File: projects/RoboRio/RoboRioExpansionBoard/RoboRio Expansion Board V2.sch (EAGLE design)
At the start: 82 parts, among them J1 RRINTERFACE-FEMALE, J2 MICROSD, Q1 5.0 MHz, T1 NPN-SOT416, U1 P8X32A-Q44, U2 24LC256ST, U3 FT232RFTR232R, U4 MC1525TO

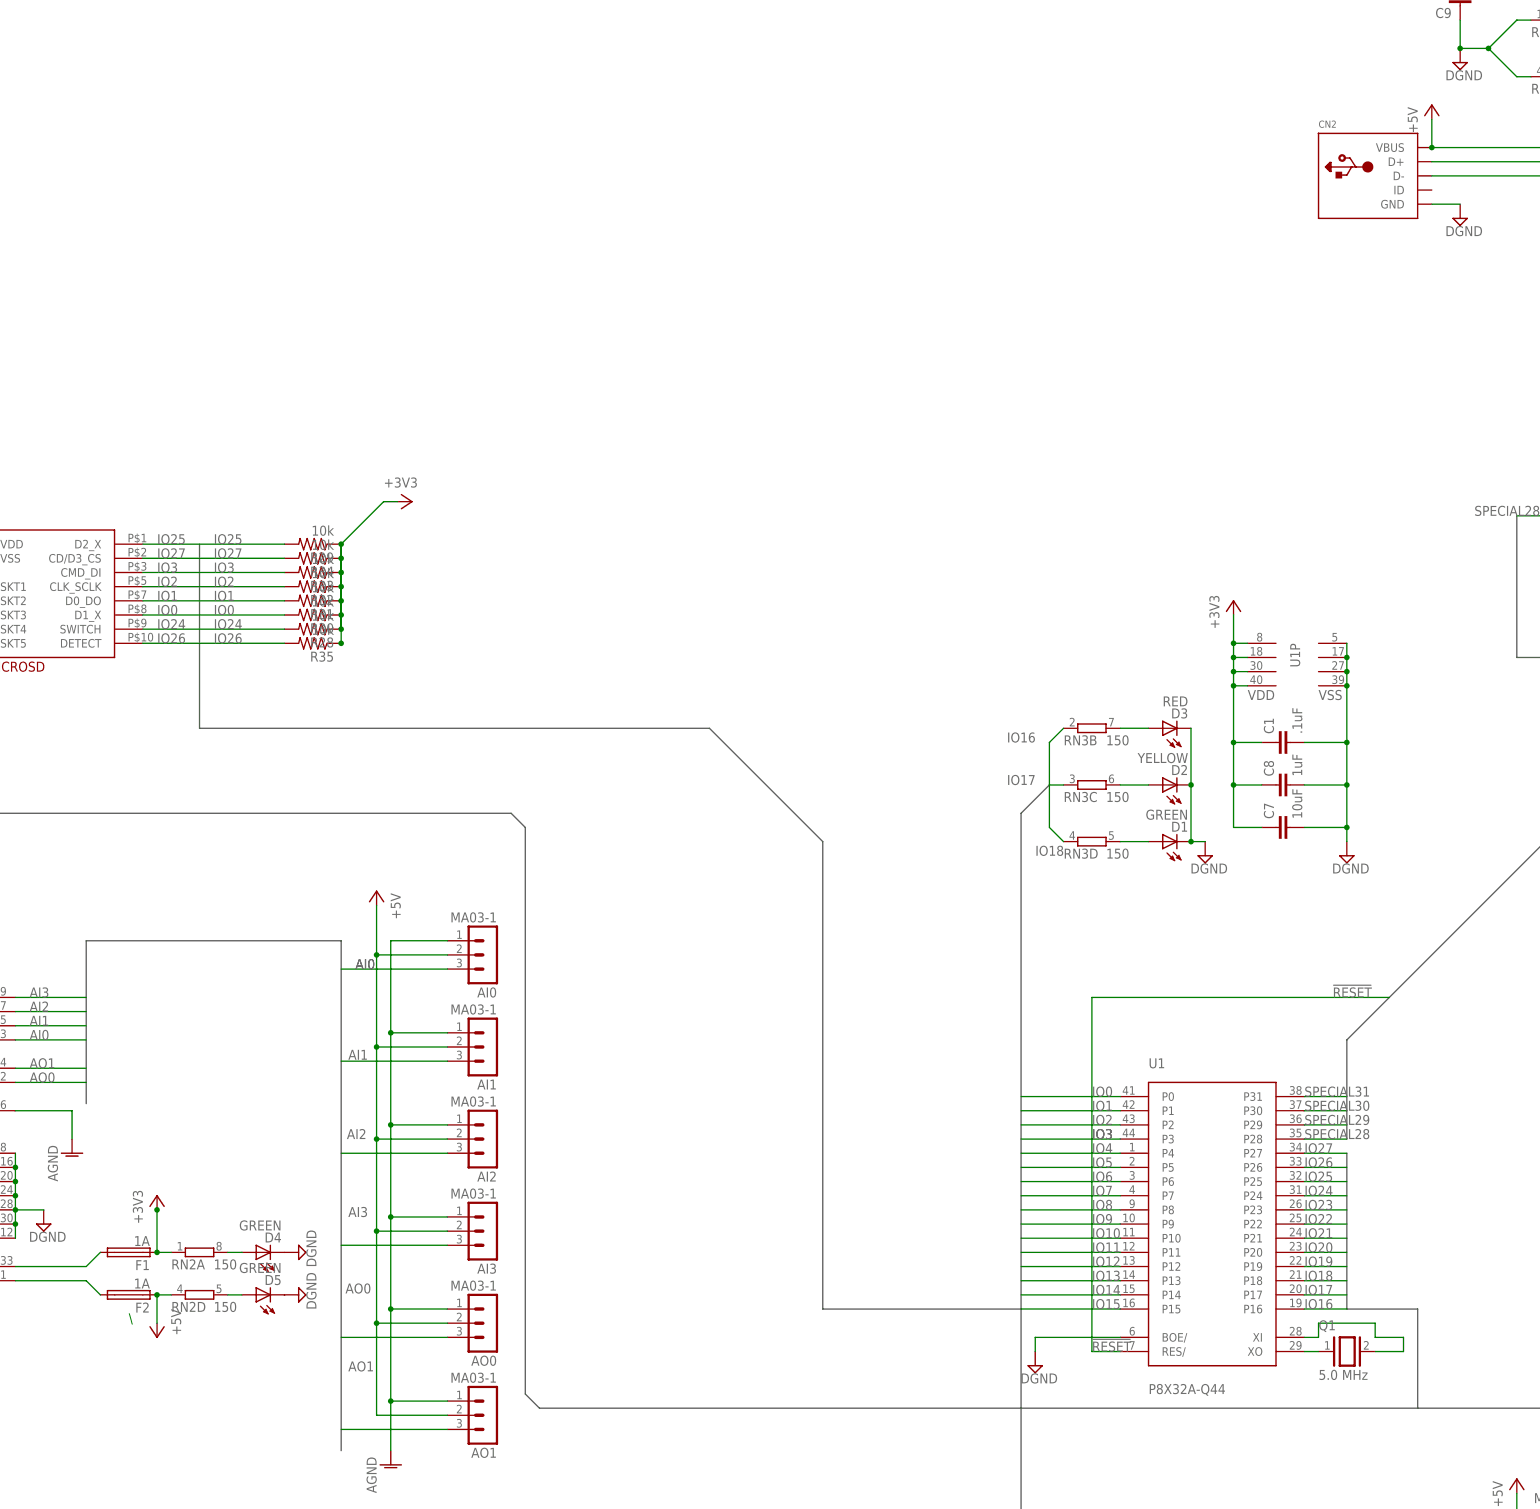
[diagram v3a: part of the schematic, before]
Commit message: Small changes
Made more space by moving stuff around
USB 5V is no longer directly tied to RR 5V
Removed fuses
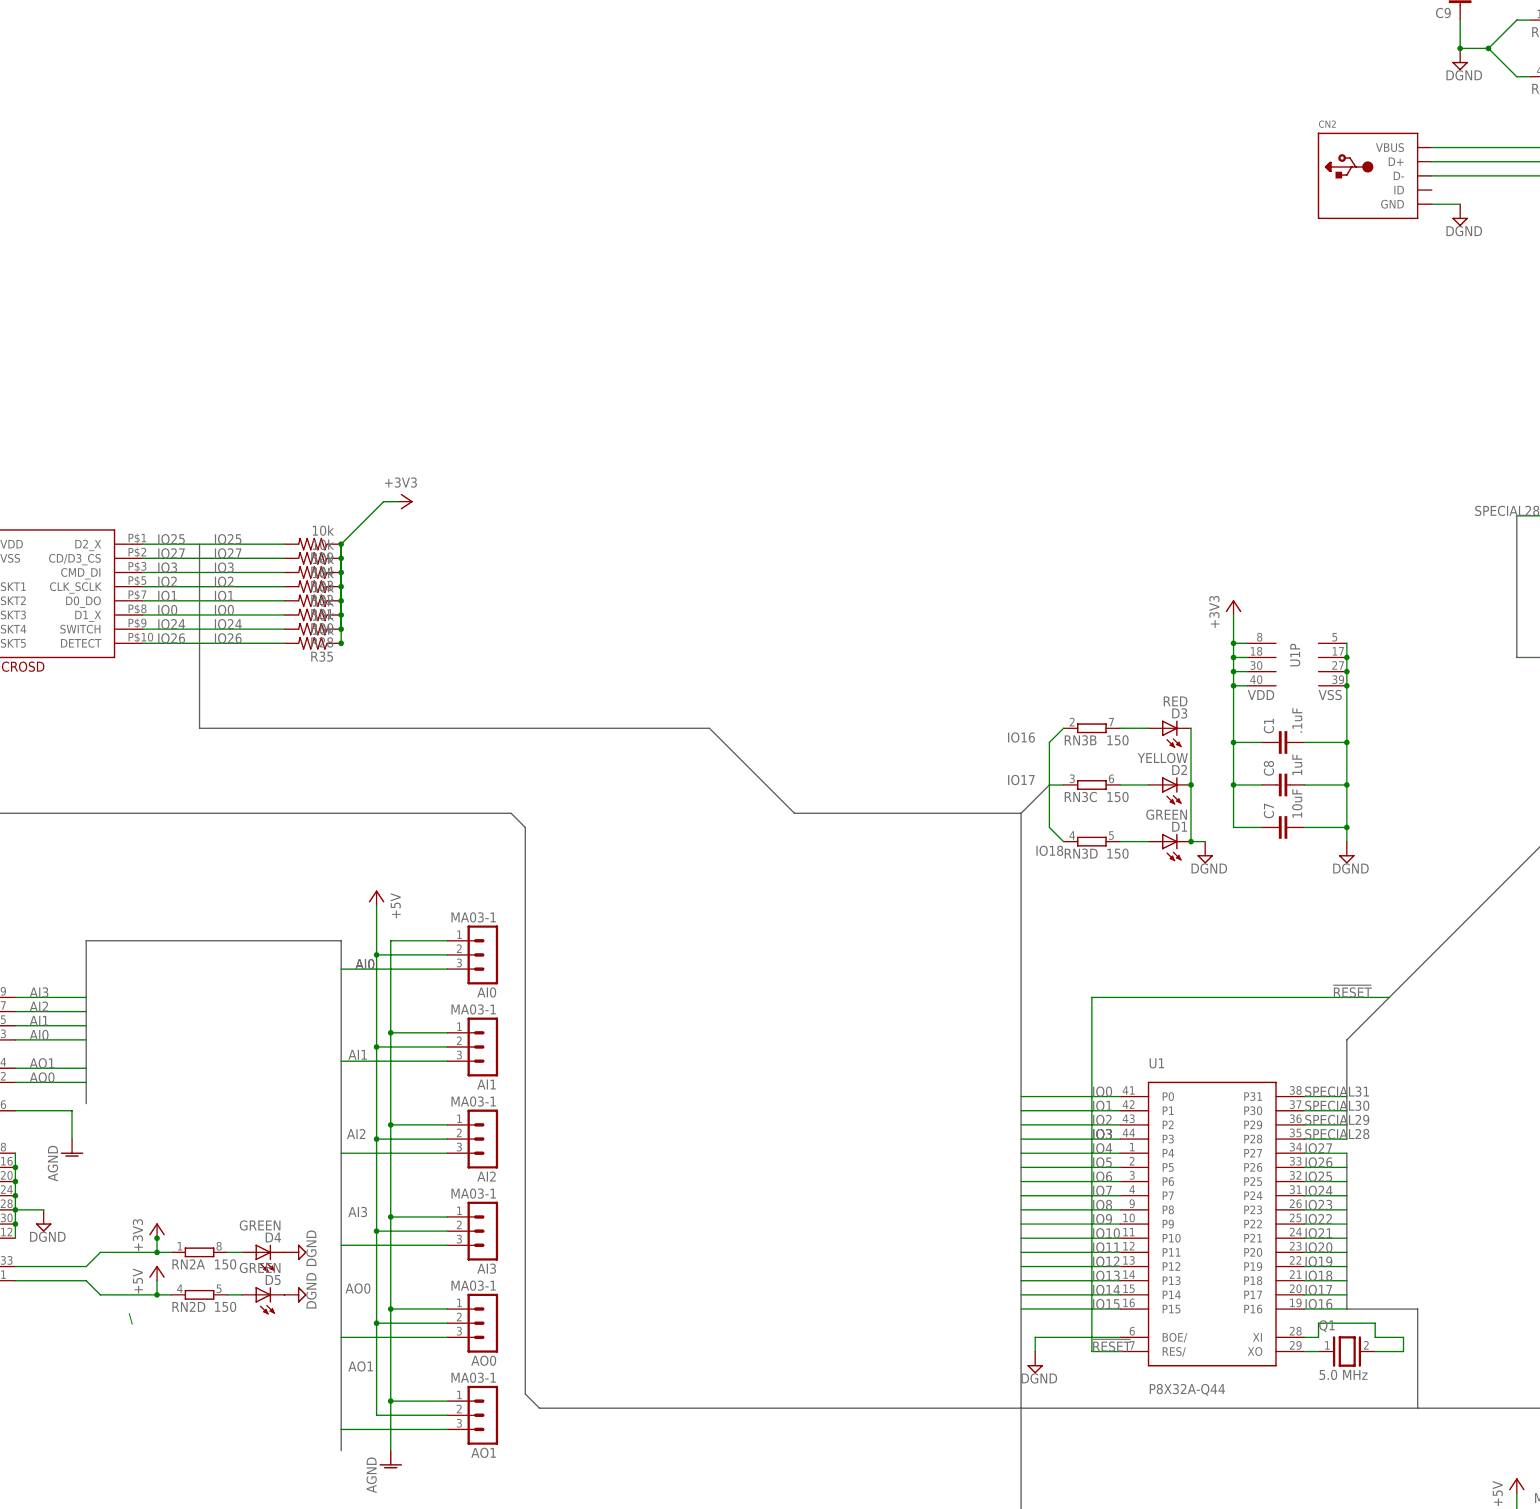
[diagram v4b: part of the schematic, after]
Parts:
- removed F1, F2: 1A, fuse:TR5
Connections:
- removed net N$15: F2.2, J1.P1-5V
- net +3V3: now also J1.P33-+3.3V; no longer F1.1
- net +5V: now also J1.P1-5V; no longer CN2.VBUS, F2.1, U3.VCC
- net N$5: now also CN2.VBUS, U3.VCC; no longer F1.2, J1.P33-+3.3V
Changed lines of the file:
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@@
 <part name="ADC7" library="con-lstb-modified" deviceset="MA03-1" device=""/>
 <part name="P+14" library="supply1" deviceset="+5V" device=""/>
-<part name="F2" library="fuse" deviceset="TR5" device="" value="1A"/>
-<part name="F1" library="fuse" deviceset="TR5" device="" value="1A"/>
 <part name="D4" library="led" deviceset="LED" device="CHIPLED_0603" value="GREEN"/>
 <part name="D5" library="led" deviceset="LED" device="CHIPLED_0603" value="GREEN"/>
@@
 <part name="U5" library="MAX11621EEE" deviceset="MAXIM1152" device="SMT"/>
 <part name="CN2" library="adafruit" deviceset="USB" device="MINIB"/>
-<part name="P+1" library="supply1" deviceset="+5V" device=""/>
 <part name="U3" library="FT232R" deviceset="FT232R" device="FTR232R"/>
 <part name="C9" library="resistor" deviceset="C-EU" device="C0603K" value="1uF"/>
@@
 <instance part="ADC7" gate="G$1" x="271.78" y="-66.04" rot="R180"/>
 <instance part="P+14" gate="1" x="256.54" y="-59.69"/>
-<instance part="F2" gate="1" x="-160.02" y="20.32" rot="R180"/>
-<instance part="F1" gate="1" x="-160.02" y="27.94" rot="R180"/>
 <instance part="D4" gate="G$1" x="-137.16" y="27.94" rot="R90"/>
 <instance part="D5" gate="G$1" x="-137.16" y="20.32" rot="R90"/>
 <instance part="SUPPLY39" gate="G$1" x="-129.54" y="20.32" rot="R90"/>
 <instance part="SUPPLY40" gate="G$1" x="-129.54" y="27.94" rot="R90"/>
-<instance part="+3V7" gate="G$1" x="-154.94" y="38.1"/>
-<instance part="P+16" gate="1" x="-154.94" y="12.7" rot="R180"/>
+<instance part="+3V7" gate="G$1" x="-154.94" y="33.02"/>
+<instance part="P+16" gate="1" x="-154.94" y="25.4"/>
 <instance part="GPIO0" gate="G$1" x="127" y="66.04" rot="R180"/>
 <instance part="+3V3" gate="G$1" x="116.84" y="66.04" rot="R90"/>
@@
 <instance part="U5" gate="G$1" x="88.9" y="-76.2"/>
 <instance part="CN2" gate="G$1" x="63.5" y="220.98"/>
-<instance part="P+1" gate="1" x="73.66" y="233.68"/>
 <instance part="U3" gate="G$1" x="134.62" y="231.14"/>
 <instance part="C9" gate="G$1" x="78.74" y="251.46" rot="R180"/>
@@
 <wire x1="101.6" y1="0" x2="71.12" y2="0" width="0.762" layer="92"/>
 <wire x1="71.12" y1="0" x2="0" y2="0" width="0.762" layer="92"/>
-<wire x1="0" y1="0" x2="0" y2="17.78" width="0.762" layer="92"/>
-<wire x1="0" y1="17.78" x2="0" y2="106.68" width="0.762" layer="92"/>
+<wire x1="0" y1="0" x2="0" y2="106.68" width="0.762" layer="92"/>
 <wire x1="0" y1="106.68" x2="5.08" y2="111.76" width="0.762" layer="92"/>
 <wire x1="0" y1="0" x2="-86.36" y2="0" width="0.762" layer="92"/>
 <wire x1="-86.36" y1="0" x2="-88.9" y2="2.54" width="0.762" layer="92"/>
 <wire x1="-88.9" y1="2.54" x2="-88.9" y2="104.14" width="0.762" layer="92"/>
-<wire x1="-35.56" y1="17.78" x2="0" y2="17.78" width="0.762" layer="92"/>
+<wire x1="-40.64" y1="106.68" x2="0" y2="106.68" width="0.762" layer="92"/>
 <wire x1="0" y1="0" x2="0" y2="-50.8" width="0.762" layer="92"/>
 <wire x1="101.6" y1="0" x2="162.56" y2="0" width="0.762" layer="92"/>
@@
 <wire x1="71.12" y1="17.78" x2="58.42" y2="17.78" width="0.762" layer="92"/>
 <wire x1="58.42" y1="17.78" x2="58.42" y2="45.72" width="0.762" layer="92"/>
-<wire x1="-35.56" y1="17.78" x2="-35.56" y2="101.6" width="0.762" layer="92"/>
-<wire x1="-35.56" y1="101.6" x2="-55.88" y2="121.92" width="0.762" layer="92"/>
+<wire x1="-40.64" y1="106.68" x2="-55.88" y2="121.92" width="0.762" layer="92"/>
 <wire x1="-55.88" y1="121.92" x2="-147.32" y2="121.92" width="0.762" layer="92"/>
 <wire x1="-147.32" y1="121.92" x2="-147.32" y2="154.94" width="0.762" layer="92"/>
@@
 <pinref part="+3V7" gate="G$1" pin="+3V3"/>
 <pinref part="+3V7" gate="G$1" pin="+3V3"/>
-<pinref part="F1" gate="1" pin="1"/>
+<wire x1="-152.4" y1="27.94" x2="-154.94" y2="27.94" width="0.1524" layer="91"/>
+<wire x1="-154.94" y1="27.94" x2="-154.94" y2="30.48" width="0.1524" layer="91"/>
+<junction x="-154.94" y="30.48"/>
+<pinref part="RN2" gate="A" pin="1"/>
+<pinref part="J1" gate="G$1" pin="P33-+3.3V"/>
+<wire x1="-180.34" y1="25.4" x2="-167.64" y2="25.4" width="0.1524" layer="91"/>
+<wire x1="-167.64" y1="25.4" x2="-165.1" y2="27.94" width="0.1524" layer="91"/>
+<wire x1="-154.94" y1="27.94" x2="-165.1" y2="27.94" width="0.1524" layer="91"/>
 <junction x="-154.94" y="27.94"/>
-<wire x1="-152.4" y1="27.94" x2="-154.94" y2="27.94" width="0.1524" layer="91"/>
-<wire x1="-154.94" y1="27.94" x2="-154.94" y2="35.56" width="0.1524" layer="91"/>
-<junction x="-154.94" y="35.56"/>
-<pinref part="RN2" gate="A" pin="1"/>
 </segment>
 <segment>
@@
 </segment>
 <segment>
-<pinref part="F2" gate="1" pin="1"/>
-<junction x="-154.94" y="20.32"/>
 <pinref part="P+16" gate="1" pin="+5V"/>
 <wire x1="-152.4" y1="20.32" x2="-154.94" y2="20.32" width="0.1524" layer="91"/>
-<wire x1="-154.94" y1="20.32" x2="-154.94" y2="15.24" width="0.1524" layer="91"/>
+<wire x1="-154.94" y1="20.32" x2="-154.94" y2="22.86" width="0.1524" layer="91"/>
 <pinref part="RN2" gate="D" pin="1"/>
-</segment>
-<segment>
-<pinref part="CN2" gate="G$1" pin="VBUS"/>
-<pinref part="P+1" gate="1" pin="+5V"/>
-<wire x1="73.66" y1="231.14" x2="73.66" y2="226.06" width="0.1524" layer="91"/>
-<junction x="73.66" y="226.06"/>
-<pinref part="U3" gate="G$1" pin="VCC"/>
-<wire x1="116.84" y1="228.6" x2="119.38" y2="228.6" width="0.1524" layer="91"/>
-<wire x1="73.66" y1="226.06" x2="114.3" y2="226.06" width="0.1524" layer="91"/>
-<wire x1="114.3" y1="226.06" x2="116.84" y2="228.6" width="0.1524" layer="91"/>
+<pinref part="J1" gate="G$1" pin="P1-5V"/>
+<wire x1="-180.34" y1="22.86" x2="-167.64" y2="22.86" width="0.1524" layer="91"/>
+<wire x1="-167.64" y1="22.86" x2="-165.1" y2="20.32" width="0.1524" layer="91"/>
+<wire x1="-165.1" y1="20.32" x2="-154.94" y2="20.32" width="0.1524" layer="91"/>
+<junction x="-154.94" y="20.32"/>
 </segment>
 <segment>
@@
 </segment>
 </net>
-<net name="N$15" class="0">
-<segment>
-<pinref part="J1" gate="G$1" pin="P1-5V"/>
-<wire x1="-180.34" y1="22.86" x2="-167.64" y2="22.86" width="0.1524" layer="91"/>
-<wire x1="-167.64" y1="22.86" x2="-165.1" y2="20.32" width="0.1524" layer="91"/>
-<pinref part="F2" gate="1" pin="2"/>
-</segment>
-</net>
 <net name="IO4" class="0">
 <segment>
@@
 <pinref part="ADC1" gate="G$1" pin="3"/>
 <wire x1="134.62" y1="-121.92" x2="205.74" y2="-121.92" width="0.1524" layer="91"/>
-</segment>
-</net>
-<net name="N$5" class="0">
-<segment>
-<pinref part="J1" gate="G$1" pin="P33-+3.3V"/>
-<wire x1="-180.34" y1="25.4" x2="-167.64" y2="25.4" width="0.1524" layer="91"/>
-<wire x1="-167.64" y1="25.4" x2="-165.1" y2="27.94" width="0.1524" layer="91"/>
-<pinref part="F1" gate="1" pin="2"/>
 </segment>
 </net>
@@
 </segment>
 </net>
+<net name="N$5" class="0">
+<segment>
+<pinref part="CN2" gate="G$1" pin="VBUS"/>
+<pinref part="U3" gate="G$1" pin="VCC"/>
+<wire x1="116.84" y1="228.6" x2="119.38" y2="228.6" width="0.1524" layer="91"/>
+<wire x1="73.66" y1="226.06" x2="114.3" y2="226.06" width="0.1524" layer="91"/>
+<wire x1="114.3" y1="226.06" x2="116.84" y2="228.6" width="0.1524" layer="91"/>
+</segment>
+</net>

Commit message: Changed every 3 pin connection to the new symbol, attached connections properly
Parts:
- removed ADC0, ADC1, ADC2, ADC3, ADC4, ADC5, ADC6, ADC7, AI0, AI1, AI2, AI3, AO0, AO1, GPIO0, GPIO1, GPIO2, GPIO3, IOCLK, IOCS, IOMISO, IOMOSI, IORX, IOSCL, IOSDA, IOTX, LCD: MA03-1, con-lstb-modified:MA03-1
- added U$13, U$14, U$15, U$16, U$17, U$18, U$19, U$20, U$21, U$22, U$23, U$24, U$25, U$26, U$27, U$28, U$29, U$3, U$30, U$31, U$32, U$33, U$34, U$35, U$36, U$37, U$4: 3PINDEVICEDEFAULT, 3pin:3PINDEVICEDEFAULT
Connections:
- net +3V3: now also U$25.V+, U$26.V+, U$27.V+, U$28.V+, U$29.V+, U$30.V+, U$31.V+, U$32.V+, U$33.V+, U$34.V+, U$35.V+, U$36.V+; no longer GPIO0.2, GPIO1.2, GPIO2.2, GPIO3.2, IOCLK.2, IOCS.2, IOMISO.2, IOMOSI.2, IORX.2, IOSCL.2, IOSDA.2, IOTX.2
- net +5V: now also U$13.V+, U$14.V+, U$15.V+, U$16.V+, U$18.V+, U$19.V+, U$20.V+, U$21.V+, U$22.V+, U$23.V+, U$24.V+, U$3.V+, U$37.V+, U$4.V+; no longer ADC0.2, ADC1.2, ADC2.2, ADC3.2, ADC4.2, ADC5.2, ADC6.2, ADC7.2, AI0.2, AI1.2, AI2.2, AI3.2, AO0.2, AO1.2, LCD.2
- net AGND: no longer AI0.1, AI1.1, AI2.1, AI3.1, AO0.1, AO1.1
- net AI0: now also U$3.DATA; no longer AI0.3
- net AI1: now also U$4.DATA; no longer AI1.3
- net AI2: now also U$13.DATA; no longer AI2.3
- net AI3: now also U$14.DATA; no longer AI3.3
- net AO0: now also U$15.DATA; no longer AO0.3
- net AO1: now also U$16.DATA; no longer AO1.3
- net DGND: now also U$13.GND, U$14.GND, U$15.GND, U$16.GND, U$17.GND, U$18.GND, U$19.GND, U$20.GND, U$21.GND, U$22.GND, U$23.GND, U$24.GND, U$25.GND, U$26.GND, U$27.GND, U$28.GND, U$29.GND, U$3.GND, U$30.GND, U$31.GND, U$32.GND, U$33.GND, U$34.GND, U$35.GND, U$36.GND, U$37.GND, U$4.GND; no longer ADC0.1, ADC1.1, ADC2.1, ADC3.1, ADC4.1, ADC5.1, ADC6.1, ADC7.1, GPIO0.1, GPIO1.1, GPIO2.1, GPIO3.1, IOCLK.1, IOCS.1, IOMISO.1, IOMOSI.1, IORX.1, IOSCL.1, IOSDA.1, IOTX.1, LCD.1
- net IO10: now also U$32.DATA; no longer IOCLK.3
- net IO11: now also U$36.DATA; no longer IOMISO.3
- net IO12: now also U$35.DATA; no longer IOMOSI.3
- net IO13: now also U$34.DATA; no longer IOSCL.3
- net IO14: now also U$33.DATA; no longer IOSDA.3
- net IO15: now also U$37.DATA; no longer LCD.3
- net IO19: now also U$25.DATA; no longer GPIO3.3
- net IO4: now also U$28.DATA; no longer GPIO0.3
- net IO5: now also U$27.DATA; no longer GPIO1.3
- net IO6: now also U$26.DATA; no longer GPIO2.3
- net IO7: now also U$29.DATA; no longer IOTX.3
- net IO8: now also U$30.DATA; no longer IORX.3
- net IO9: now also U$31.DATA; no longer IOCS.3
- net N$10: now also U$24.DATA; no longer ADC3.3
- net N$16: no longer ADC2.3
- net N$17: now also U$23.DATA; no longer ADC4.3
- net N$30: now also U$22.DATA; no longer ADC5.3
- net N$34: now also U$20.DATA; no longer ADC7.3
- net N$40: now also U$21.DATA; no longer ADC6.3
- net N$8: now also U$19.DATA; no longer ADC0.3
- net N$9: now also U$18.DATA; no longer ADC1.3
